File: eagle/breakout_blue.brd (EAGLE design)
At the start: 28.6 x 28.6 mm, 18 parts, among them X1 734120110

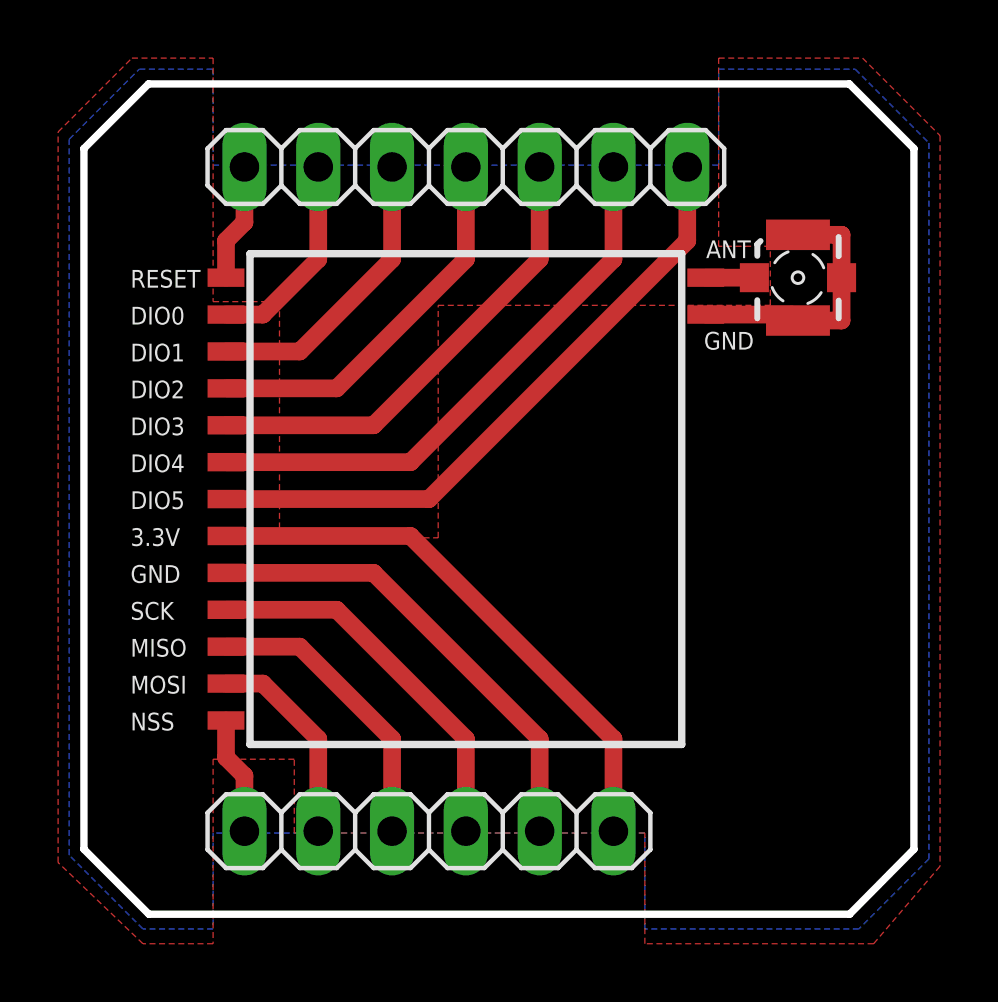
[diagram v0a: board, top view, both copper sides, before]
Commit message: Shield and breakout layout update
Added a gap to the pin headers on LoRa breakout board and the shield to enforce breakout orientation.
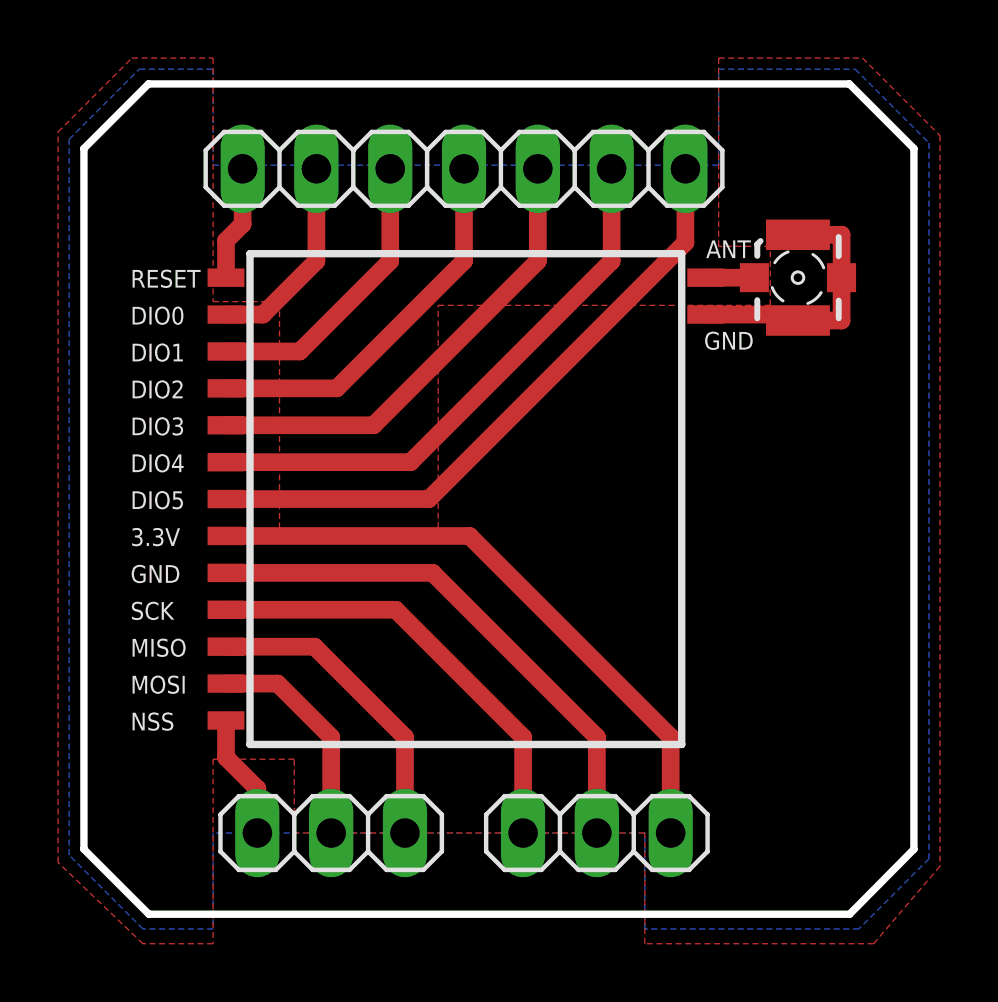
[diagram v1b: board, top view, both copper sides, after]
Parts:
- removed JP2: (no value), pinhead:1X06
- added JP2A, JP2B: (no value), pinhead:1X03
- moved JP1 0.09 mm to (13.1, 25.7)
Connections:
- net 3.3V: now also JP2A.1; no longer JP2.1
- net GND: now also JP2A.2; no longer JP2.2
- net MISO: now also JP2B.1; no longer JP2.4
- net MOSI: now also JP2B.2; no longer JP2.5
- net NSS: now also JP2B.3; no longer JP2.6
- net SCK: now also JP2A.3; no longer JP2.3
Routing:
- net GND: track 25.5 -> 27.6 mm
- net 3.3V: track 19.4 -> 21.5 mm
- net SCK: track 13.3 -> 15.3 mm
- net MISO: track 10.2 -> 10.8 mm
- net MOSI: track 7.14 -> 7.68 mm
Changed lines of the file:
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@@
 </autorouter>
 <elements>
-<element name="JP1" library="pinhead" package="1X07" value="" x="13.1445" y="25.7175" smashed="yes">
-<attribute name="VALUE" x="4.2545" y="22.5425" size="1.27" layer="27"/>
-</element>
-<element name="JP2" library="pinhead" package="1X06" value="" x="11.8745" y="2.8575" smashed="yes" rot="R180">
-<attribute name="VALUE" x="19.4945" y="6.0325" size="1.27" layer="27" rot="R180"/>
+<element name="JP1" library="pinhead" package="1X07" value="" x="13.081" y="25.654" smashed="yes">
+<attribute name="VALUE" x="4.191" y="22.479" size="1.27" layer="27"/>
 </element>
 <element name="RESET" library="wirepad" package="SMD0,65-1,27" value="" x="4.8895" y="21.9075" smashed="yes" rot="R270">
@@
 </element>
 <element name="X1" library="con-coax" package="734120110" value="734120110" x="24.5745" y="21.9075" smashed="yes" rot="R270"/>
+<element name="JP2A" library="pinhead" package="1X03" value="" x="17.653" y="2.794" smashed="yes" rot="R180">
+<attribute name="VALUE" x="21.463" y="5.969" size="1.27" layer="27" rot="R180"/>
+</element>
+<element name="JP2B" library="pinhead" package="1X03" value="" x="8.509" y="2.794" smashed="yes" rot="R180">
+<attribute name="VALUE" x="12.319" y="5.969" size="1.27" layer="27" rot="R180"/>
+</element>
 </elements>
 <signals>
@@
 <contactref element="JP1" pad="1"/>
 <contactref element="RESET" pad="1"/>
-<wire x1="5.5245" y1="25.7175" x2="5.5245" y2="23.8125" width="0.6096" layer="1"/>
-<wire x1="5.5245" y1="23.8125" x2="4.8895" y2="23.1775" width="0.6096" layer="1"/>
 <wire x1="4.8895" y1="23.1775" x2="4.8895" y2="21.9075" width="0.6096" layer="1"/>
+<wire x1="5.461" y1="25.654" x2="5.461" y2="23.749" width="0.6096" layer="1"/>
+<wire x1="5.461" y1="23.749" x2="4.8895" y2="23.1775" width="0.6096" layer="1"/>
 </signal>
 <signal name="DIO0">
 <contactref element="JP1" pad="2"/>
 <contactref element="DIO0" pad="1"/>
-<wire x1="8.0645" y1="25.7175" x2="8.0645" y2="22.5425" width="0.6096" layer="1"/>
-<wire x1="8.0645" y1="22.5425" x2="6.1595" y2="20.6375" width="0.6096" layer="1"/>
 <wire x1="6.1595" y1="20.6375" x2="4.8895" y2="20.6375" width="0.6096" layer="1"/>
+<wire x1="8.001" y1="25.654" x2="8.001" y2="22.479" width="0.6096" layer="1"/>
+<wire x1="8.001" y1="22.479" x2="6.1595" y2="20.6375" width="0.6096" layer="1"/>
 </signal>
 <signal name="DIO1">
 <contactref element="JP1" pad="3"/>
 <contactref element="DIO1" pad="1"/>
-<wire x1="4.8895" y1="19.3675" x2="7.4295" y2="19.3675" width="0.6096" layer="1"/>
-<wire x1="7.4295" y1="19.3675" x2="10.6045" y2="22.5425" width="0.6096" layer="1"/>
-<wire x1="10.6045" y1="22.5425" x2="10.6045" y2="25.7175" width="0.6096" layer="1"/>
+<wire x1="7.4295" y1="19.3675" x2="4.8895" y2="19.3675" width="0.6096" layer="1"/>
+<wire x1="10.541" y1="25.654" x2="10.541" y2="22.479" width="0.6096" layer="1"/>
+<wire x1="10.541" y1="22.479" x2="7.4295" y2="19.3675" width="0.6096" layer="1"/>
 </signal>
 <signal name="DIO3">
 <contactref element="JP1" pad="5"/>
 <contactref element="DIO3" pad="1"/>
-<wire x1="4.8895" y1="16.8275" x2="9.9695" y2="16.8275" width="0.6096" layer="1"/>
-<wire x1="9.9695" y1="16.8275" x2="15.6845" y2="22.5425" width="0.6096" layer="1"/>
-<wire x1="15.6845" y1="22.5425" x2="15.6845" y2="25.7175" width="0.6096" layer="1"/>
+<wire x1="9.9695" y1="16.8275" x2="4.8895" y2="16.8275" width="0.6096" layer="1"/>
+<wire x1="15.621" y1="25.654" x2="15.621" y2="22.479" width="0.6096" layer="1"/>
+<wire x1="15.621" y1="22.479" x2="9.9695" y2="16.8275" width="0.6096" layer="1"/>
 </signal>
 <signal name="DIO4">
 <contactref element="JP1" pad="6"/>
 <contactref element="DIO4" pad="1"/>
-<wire x1="4.8895" y1="15.5575" x2="11.2395" y2="15.5575" width="0.6096" layer="1"/>
-<wire x1="11.2395" y1="15.5575" x2="18.2245" y2="22.5425" width="0.6096" layer="1"/>
-<wire x1="18.2245" y1="22.5425" x2="18.2245" y2="25.7175" width="0.6096" layer="1"/>
+<wire x1="11.2395" y1="15.5575" x2="4.8895" y2="15.5575" width="0.6096" layer="1"/>
+<wire x1="18.161" y1="25.654" x2="18.161" y2="22.479" width="0.6096" layer="1"/>
+<wire x1="18.161" y1="22.479" x2="11.2395" y2="15.5575" width="0.6096" layer="1"/>
 </signal>
 <signal name="DIO5">
 <contactref element="JP1" pad="7"/>
 <contactref element="DIO5" pad="1"/>
-<wire x1="20.7645" y1="25.7175" x2="20.7645" y2="23.1775" width="0.6096" layer="1"/>
-<wire x1="20.7645" y1="23.1775" x2="11.8745" y2="14.2875" width="0.6096" layer="1"/>
 <wire x1="11.8745" y1="14.2875" x2="4.8895" y2="14.2875" width="0.6096" layer="1"/>
+<wire x1="20.701" y1="25.654" x2="20.701" y2="23.114" width="0.6096" layer="1"/>
+<wire x1="20.701" y1="23.114" x2="11.8745" y2="14.2875" width="0.6096" layer="1"/>
 </signal>
 <signal name="3.3V">
 <contactref element="3.3V" pad="1"/>
-<wire x1="18.2245" y1="6.0325" x2="11.2395" y2="13.0175" width="0.6096" layer="1"/>
-<wire x1="11.2395" y1="13.0175" x2="4.8895" y2="13.0175" width="0.6096" layer="1"/>
-<contactref element="JP2" pad="1"/>
-<wire x1="18.2245" y1="6.0325" x2="18.2245" y2="2.8575" width="0.6096" layer="1"/>
+<wire x1="13.2715" y1="13.0175" x2="4.8895" y2="13.0175" width="0.6096" layer="1"/>
+<contactref element="JP2A" pad="1"/>
+<wire x1="20.193" y1="2.794" x2="20.193" y2="6.096" width="0.6096" layer="1"/>
+<wire x1="20.193" y1="6.096" x2="13.2715" y2="13.0175" width="0.6096" layer="1"/>
 </signal>
 <signal name="SCK">
 <contactref element="SCK" pad="1"/>
-<wire x1="13.1445" y1="6.0325" x2="8.6995" y2="10.4775" width="0.6096" layer="1"/>
-<wire x1="8.6995" y1="10.4775" x2="4.8895" y2="10.4775" width="0.6096" layer="1"/>
-<contactref element="JP2" pad="3"/>
-<wire x1="13.1445" y1="6.0325" x2="13.1445" y2="2.8575" width="0.6096" layer="1"/>
+<wire x1="10.7315" y1="10.4775" x2="4.8895" y2="10.4775" width="0.6096" layer="1"/>
+<contactref element="JP2A" pad="3"/>
+<wire x1="15.113" y1="2.794" x2="15.113" y2="6.096" width="0.6096" layer="1"/>
+<wire x1="15.113" y1="6.096" x2="10.7315" y2="10.4775" width="0.6096" layer="1"/>
 </signal>
 <signal name="MISO">
 <contactref element="MISO" pad="1"/>
-<wire x1="4.8895" y1="9.2075" x2="7.4295" y2="9.2075" width="0.6096" layer="1"/>
-<wire x1="7.4295" y1="9.2075" x2="10.6045" y2="6.0325" width="0.6096" layer="1"/>
-<contactref element="JP2" pad="4"/>
-<wire x1="10.6045" y1="6.0325" x2="10.6045" y2="2.8575" width="0.6096" layer="1"/>
+<wire x1="7.9375" y1="9.2075" x2="4.8895" y2="9.2075" width="0.6096" layer="1"/>
+<contactref element="JP2B" pad="1"/>
+<wire x1="11.049" y1="2.794" x2="11.049" y2="6.096" width="0.6096" layer="1"/>
+<wire x1="11.049" y1="6.096" x2="7.9375" y2="9.2075" width="0.6096" layer="1"/>
 </signal>
 <signal name="MOSI">
 <contactref element="MOSI" pad="1"/>
-<wire x1="4.8895" y1="7.9375" x2="6.1595" y2="7.9375" width="0.6096" layer="1"/>
-<wire x1="6.1595" y1="7.9375" x2="8.0645" y2="6.0325" width="0.6096" layer="1"/>
-<contactref element="JP2" pad="5"/>
-<wire x1="8.0645" y1="6.0325" x2="8.0645" y2="2.8575" width="0.6096" layer="1"/>
+<wire x1="6.6675" y1="7.9375" x2="4.8895" y2="7.9375" width="0.6096" layer="1"/>
+<contactref element="JP2B" pad="2"/>
+<wire x1="8.509" y1="2.794" x2="8.509" y2="6.096" width="0.6096" layer="1"/>
+<wire x1="8.509" y1="6.096" x2="6.6675" y2="7.9375" width="0.6096" layer="1"/>
 </signal>
 <signal name="NSS">
 <contactref element="NSS" pad="1"/>
-<wire x1="4.8895" y1="6.6675" x2="4.8895" y2="5.3975" width="0.6096" layer="1"/>
-<wire x1="4.8895" y1="5.3975" x2="5.5245" y2="4.7625" width="0.6096" layer="1"/>
-<contactref element="JP2" pad="6"/>
-<wire x1="5.5245" y1="4.7625" x2="5.5245" y2="2.8575" width="0.6096" layer="1"/>
+<wire x1="4.8895" y1="5.3975" x2="4.8895" y2="6.6675" width="0.6096" layer="1"/>
+<contactref element="JP2B" pad="3"/>
+<wire x1="5.969" y1="2.794" x2="5.969" y2="4.318" width="0.6096" layer="1"/>
+<wire x1="5.969" y1="4.318" x2="4.8895" y2="5.3975" width="0.6096" layer="1"/>
 </signal>
 <signal name="ANT">
@@
 <signal name="GND" airwireshidden="yes">
 <contactref element="GND" pad="1"/>
-<wire x1="15.6845" y1="6.0325" x2="9.9695" y2="11.7475" width="0.6096" layer="1"/>
-<wire x1="9.9695" y1="11.7475" x2="4.8895" y2="11.7475" width="0.6096" layer="1"/>
-<contactref element="JP2" pad="2"/>
-<wire x1="15.6845" y1="6.0325" x2="15.6845" y2="2.8575" width="0.6096" layer="1"/>
+<wire x1="12.0015" y1="11.7475" x2="4.8895" y2="11.7475" width="0.6096" layer="1"/>
 <contactref element="GND_A" pad="1"/>
 <contactref element="X1" pad="S@1"/>
@@
 <vertex x="-0.508" y="26.67"/>
 </polygon>
-<wire x1="21.3995" y1="20.6375" x2="9.9695" y2="11.7475" width="0" layer="19" extent="1-1"/>
+<contactref element="JP2A" pad="2"/>
+<wire x1="17.653" y1="2.794" x2="17.653" y2="6.096" width="0.6096" layer="1"/>
+<wire x1="17.653" y1="6.096" x2="12.0015" y2="11.7475" width="0.6096" layer="1"/>
+<wire x1="12.0015" y1="11.7475" x2="21.3995" y2="20.6375" width="0" layer="19" extent="1-1"/>
 </signal>
 <signal name="DIO2">
 <contactref element="JP1" pad="4"/>
 <contactref element="DIO2" pad="1"/>
-<wire x1="4.8895" y1="18.0975" x2="8.6995" y2="18.0975" width="0.6096" layer="1"/>
-<wire x1="8.6995" y1="18.0975" x2="13.1445" y2="22.5425" width="0.6096" layer="1"/>
-<wire x1="13.1445" y1="22.5425" x2="13.1445" y2="25.7175" width="0.6096" layer="1"/>
+<wire x1="8.6995" y1="18.0975" x2="4.8895" y2="18.0975" width="0.6096" layer="1"/>
+<wire x1="13.081" y1="25.654" x2="13.081" y2="22.479" width="0.6096" layer="1"/>
+<wire x1="13.081" y1="22.479" x2="8.6995" y2="18.0975" width="0.6096" layer="1"/>
 </signal>
 </signals>
